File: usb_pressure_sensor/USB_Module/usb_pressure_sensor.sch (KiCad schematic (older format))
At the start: 8 parts, among them IC1 STM32F042F6P6, J1 SCREW_TERM, J2 MODULE_BRIDGE, P1 SWD_TC, U1 MICRO_USB

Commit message: Started update to different pressure sensor module
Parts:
- removed J1: SCREW_TERM, symbol CONN_01x02
- added C2: 1u, Capacitors_SMD:C_0603, symbol C
- added IC2: MCP1700, agg:SOT-23, symbol MCP1700
- added R3: 10k, Resistors_THT:R_Axial_DIN0207_L6.3mm_D2.5mm_P7.62mm_Horizontal, symbol R
- added SW1: SWITCH_SPST, symbol SWITCH_SPST
- C1: value 22u -> 1u; footprint (none) -> Capacitors_SMD:C_0603
- J2: footprint (none) -> Socket_Strips:Socket_Strip_Straight_2x03_Pitch2.54mm
- P1: footprint agg:TC2030-NL -> footprints:SWD_CONN
- R1, R2: footprint (none) -> Resistors_THT:R_Axial_DIN0207_L6.3mm_D2.5mm_P7.62mm_Horizontal
- U1: footprint (none) -> agg:MICROUSB_MOLEX_47589-0001
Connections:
- net labels added: 3v3, 5v
- net labels removed: VDD, VSS
- wire segments 25 -> 32
- no-connect marks 13 -> 11
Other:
- note added: "Capacitor should be as \nclose as possible to VOUT pin\n"
- note removed: "Need a value small enough so we \ncan have surface mount but large \nenough to be useful as a bypass\ncapacitor"
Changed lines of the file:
@@
 $EndComp
 Text Label 6150 1300 0    60   ~ 0
-VDD
+3v3
 Text Label 6150 1400 0    60   ~ 0
-VDD
+3v3
 Text Label 6150 1500 0    60   ~ 0
 GND
@@
 NoConn ~ 6400 2200
 NoConn ~ 6400 2300
-NoConn ~ 6400 2000
 NoConn ~ 6400 1900
 $Comp
@@
 F 0 "P1" H 6700 3450 50  0000 L CNN
 F 1 "SWD_TC" H 6700 3050 50  0000 L CNN
-F 2 "agg:TC2030-NL" H 6700 2950 50  0001 L CNN
+F 2 "footprints:SWD_CONN" H 6700 2950 50  0001 L CNN
 F 3 "" H 6600 3350 50  0001 C CNN
 	1    7000 3250
@@
 $EndComp
 Text Label 6600 3150 2    60   ~ 0
-VDD
+3v3
 Text Label 6600 3250 2    60   ~ 0
 NRST
@@
 NoConn ~ 7400 3350
 $Comp
-L CONN_01x02 J1
-U 1 1 59921283
-P 3400 2050
-F 0 "J1" H 3350 2150 50  0000 L CNN
-F 1 "SCREW_TERM" H 3350 1850 50  0000 L CNN
-F 2 "" H 3400 2050 50  0001 C CNN
-F 3 "" H 3400 2050 50  0001 C CNN
-	1    3400 2050
-	1    0    0    -1
-$EndComp
-Text Label 3550 2050 0    60   ~ 0
-VDD
-Text Label 3550 2150 0    60   ~ 0
-VSS
-$Comp
-L C C1
-U 1 1 5992153B
-P 4000 2100
-F 0 "C1" H 4025 2200 50  0000 L CNN
-F 1 "22u" H 4025 2000 50  0000 L CNN
-F 2 "" H 4038 1950 50  0001 C CNN
-F 3 "" H 4000 2100 50  0001 C CNN
-	1    4000 2100
-	1    0    0    -1
-$EndComp
-Text Notes 4200 2300 0    60   ~ 0
-Need a value small enough so we \ncan have surface mount but large \nenough to be useful as a bypass\ncapacitor
-$Comp
 L MICRO_USB U1
 U 1 1 59922B96
@@
 F 0 "U1" H 3300 4000 60  0000 C CNN
 F 1 "MICRO_USB" H 3500 3400 60  0000 C CNN
-F 2 "" H 3350 3700 60  0001 C CNN
+F 2 "agg:MICROUSB_MOLEX_47589-0001" H 3350 3700 60  0001 C CNN
 F 3 "" H 3350 3700 60  0001 C CNN
 	1    3350 3700
 	1    0    0    -1
 $EndComp
-NoConn ~ 3650 3500
 NoConn ~ 3650 3800
 Text Label 3700 3900 0    60   ~ 0
@@
 F 0 "R1" V 3880 3600 50  0000 C CNN
 F 1 "22" V 3800 3600 50  0000 C CNN
-F 2 "" V 3730 3600 50  0001 C CNN
+F 2 "Resistors_THT:R_Axial_DIN0207_L6.3mm_D2.5mm_P7.62mm_Horizontal" V 3730 3600 50  0001 C CNN
 F 3 "" H 3800 3600 50  0001 C CNN
 	1    3800 3600
@@
 F 0 "R2" V 3880 3700 50  0000 C CNN
 F 1 "22" V 3800 3700 50  0000 C CNN
-F 2 "" V 3730 3700 50  0001 C CNN
+F 2 "Resistors_THT:R_Axial_DIN0207_L6.3mm_D2.5mm_P7.62mm_Horizontal" V 3730 3700 50  0001 C CNN
 F 3 "" H 3800 3700 50  0001 C CNN
 	1    3800 3700
@@
 F 0 "J2" H 9100 2150 50  0000 L CNN
 F 1 "MODULE_BRIDGE" H 9100 1750 50  0000 L CNN
-F 2 "" H 9200 2050 50  0001 C CNN
+F 2 "Socket_Strips:Socket_Strip_Straight_2x03_Pitch2.54mm" H 9200 2050 50  0001 C CNN
 F 3 "" H 9200 2050 50  0001 C CNN
 	1    9200 2050
 	1    0    0    -1
 $EndComp
-Wire Wire Line
-	6150 1500 6400 1500
-Wire Wire Line
-	6400 1300 6150 1300
-Wire Wire Line
-	6400 1400 6150 1400
-Wire Wire Line
-	6400 1700 6150 1700
-Wire Wire Line
-	7600 1800 8000 1800
-Wire Wire Line
-	7600 1900 8000 1900
-Wire Wire Line
-	7600 2000 8000 2000
-Wire Wire Line
-	7600 2400 8000 2400
-Wire Wire Line
-	7600 2500 8000 2500
-Wire Wire Line
-	7600 2200 8000 2200
-Wire Wire Line
-	7600 2300 8000 2300
-Wire Wire Line
-	3500 2050 3850 2050
-Wire Wire Line
-	3500 2150 3850 2150
-Wire Wire Line
-	3850 2050 3850 1950
-Wire Wire Line
-	3850 1950 4000 1950
-Wire Wire Line
-	3850 2150 3850 2250
-Wire Wire Line
-	3850 2250 4000 2250
-Wire Wire Line
-	3650 3900 3900 3900
-Wire Wire Line
-	3950 3600 4100 3600
-Wire Wire Line
-	3950 3700 4100 3700
 Text Label 8800 2050 0    60   ~ 0
-VDD
+3v3
 Text Label 8550 2150 0    60   ~ 0
 SPI_SCLK
@@
 Text Label 9350 2150 0    60   ~ 0
 SPI_MISO
+NoConn ~ 9300 2250
+$Comp
+L SWITCH_SPST SW1
+U 1 1 599811CC
+P 5750 2000
+F 0 "SW1" H 5750 2150 50  0000 C CNN
+F 1 "SWITCH_SPST" H 5750 1900 50  0000 C CNN
+F 2 "" H 5750 2000 50  0001 C CNN
+F 3 "" H 5750 2000 50  0001 C CNN
+	1    5750 2000
+	1    0    0    -1
+$EndComp
+$Comp
+L R R3
+U 1 1 59981239
+P 6100 2300
+F 0 "R3" V 6180 2300 50  0000 C CNN
+F 1 "10k" V 6100 2300 50  0000 C CNN
+F 2 "Resistors_THT:R_Axial_DIN0207_L6.3mm_D2.5mm_P7.62mm_Horizontal" V 6030 2300 50  0001 C CNN
+F 3 "" H 6100 2300 50  0001 C CNN
+	1    6100 2300
+	1    0    0    -1
+$EndComp
+Text Label 6100 2600 0    60   ~ 0
+GND
+Text Label 5400 2000 0    60   ~ 0
+3v3
+$Comp
+L MCP1700 IC2
+U 1 1 59982B20
+P 3550 2400
+F 0 "IC2" H 3350 2500 50  0000 L CNN
+F 1 "MCP1700" H 3350 2200 50  0000 L CNN
+F 2 "agg:SOT-23" H 3350 2100 50  0001 L CNN
+F 3 "http://www.farnell.com/datasheets/1784514.pdf" H 3350 2000 50  0001 L CNN
+F 4 "1296592" H 3350 1900 50  0001 L CNN "Farnell"
+	1    3550 2400
+	1    0    0    -1
+$EndComp
+$Comp
+L C C2
+U 1 1 59982B76
+P 4050 2600
+F 0 "C2" H 4075 2700 50  0000 L CNN
+F 1 "1u" H 4075 2500 50  0000 L CNN
+F 2 "Capacitors_SMD:C_0603" H 4088 2450 50  0001 C CNN
+F 3 "" H 4050 2600 50  0001 C CNN
+	1    4050 2600
+	1    0    0    -1
+$EndComp
+Text Label 4050 2900 0    60   ~ 0
+GND
+Text Notes 4250 2700 0    60   ~ 0
+Capacitor should be as \nclose as possible to VOUT pin\n
+Text Label 3250 2750 0    60   ~ 0
+GND
+$Comp
+L C C1
+U 1 1 5998353C
+P 3000 2550
+F 0 "C1" H 3025 2650 50  0000 L CNN
+F 1 "1u" H 3025 2450 50  0000 L CNN
+F 2 "Capacitors_SMD:C_0603" H 3038 2400 50  0001 C CNN
+F 3 "" H 3000 2550 50  0001 C CNN
+	1    3000 2550
+	1    0    0    -1
+$EndComp
+Text Label 2600 2400 0    60   ~ 0
+5v
+Text Label 4250 2400 0    60   ~ 0
+3v3
+Wire Wire Line
+	6150 1500 6400 1500
+Wire Wire Line
+	6400 1300 6150 1300
+Wire Wire Line
+	6400 1400 6150 1400
+Wire Wire Line
+	6400 1700 6150 1700
+Wire Wire Line
+	7600 1800 8000 1800
+Wire Wire Line
+	7600 1900 8000 1900
+Wire Wire Line
+	7600 2000 8000 2000
+Wire Wire Line
+	7600 2400 8000 2400
+Wire Wire Line
+	7600 2500 8000 2500
+Wire Wire Line
+	7600 2200 8000 2200
+Wire Wire Line
+	7600 2300 8000 2300
+Wire Wire Line
+	3650 3900 3900 3900
+Wire Wire Line
+	3950 3600 4100 3600
+Wire Wire Line
+	3950 3700 4100 3700
 Wire Wire Line
 	9300 2150 9750 2150
@@
 Wire Wire Line
 	9000 2250 8550 2250
-NoConn ~ 9300 2250
+Wire Wire Line
+	5850 2000 6400 2000
+Wire Wire Line
+	6100 2000 6100 2150
+Connection ~ 6100 2000
+Wire Wire Line
+	6100 2450 6100 2600
+Wire Wire Line
+	5650 2000 5400 2000
+Wire Wire Line
+	3950 2400 4250 2400
+Wire Wire Line
+	4050 2400 4050 2450
+Wire Wire Line
+	4050 2750 4050 2900
+Wire Wire Line
+	3250 2500 3250 2750
+Wire Wire Line
+	2600 2400 3250 2400
+Wire Wire Line
+	3000 2700 3000 2750
+Wire Wire Line
+	3000 2750 3250 2750
+Connection ~ 3000 2400
+Connection ~ 4050 2400
+Wire Wire Line
+	3650 3500 3650 3450
+Wire Wire Line
+	3650 3450 4000 3450
+Text Label 4000 3450 0    60   ~ 0
+5v
 $EndSCHEMATC

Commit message: First iteration with new pressure sensor
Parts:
- added C3, C4: 24p, symbol C
- added R4: 2.2M, symbol R
- added R5: 180k, symbol R
- added U2: SN74LVC1GX04, symbol SN74LVC1GX04
- added Y1: Crystal 32.768kHz, symbol Crystal
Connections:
- net labels added: DIN, DOUT, MCLK, SCLK
- net labels removed: SPI_MISO, SPI_MOSI, SPI_SCLK
- wire segments 32 -> 46
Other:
- note added: "Chose 22ohm because:\nhttp://www.eevblog.com/forum/projects/why-usb-data-series-resistors/"
- note added: "Crystal Oscillator"
- note added: "Crystal Oscillator design process:\n\nFor the values used http://www.ti.com/lit/an/szza043/szza043.pdf page 13\n180k should be approx equal to capacitave reactance of one of the capacitors\n connected to gound. Used 1/j*2pi*f*C where f is the resonant freq of the \ncrystal.\n2.2M should be between 1M and 10M so I just used the one they used in the\nexample.\nThe two caps going to ground should be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"
- note added: "I'm using the SPI pins even though the pressure sesnsor doesn't say it uses SPI\nbut it should be the same concepts right?\nEven if we can't hack SPI into working these pins are still general purpose IO so\ni think it's ok?"
- note added: "MCU"
- note added: "Module Bridge"
- note added: "Power Supply"
- note added: "Serial Wire Debugging"
- note added: "USB Interface"
- moved on the sheet: C1, C2, IC1, IC2, J2, P1, R1, R2, R3, SW1, U1

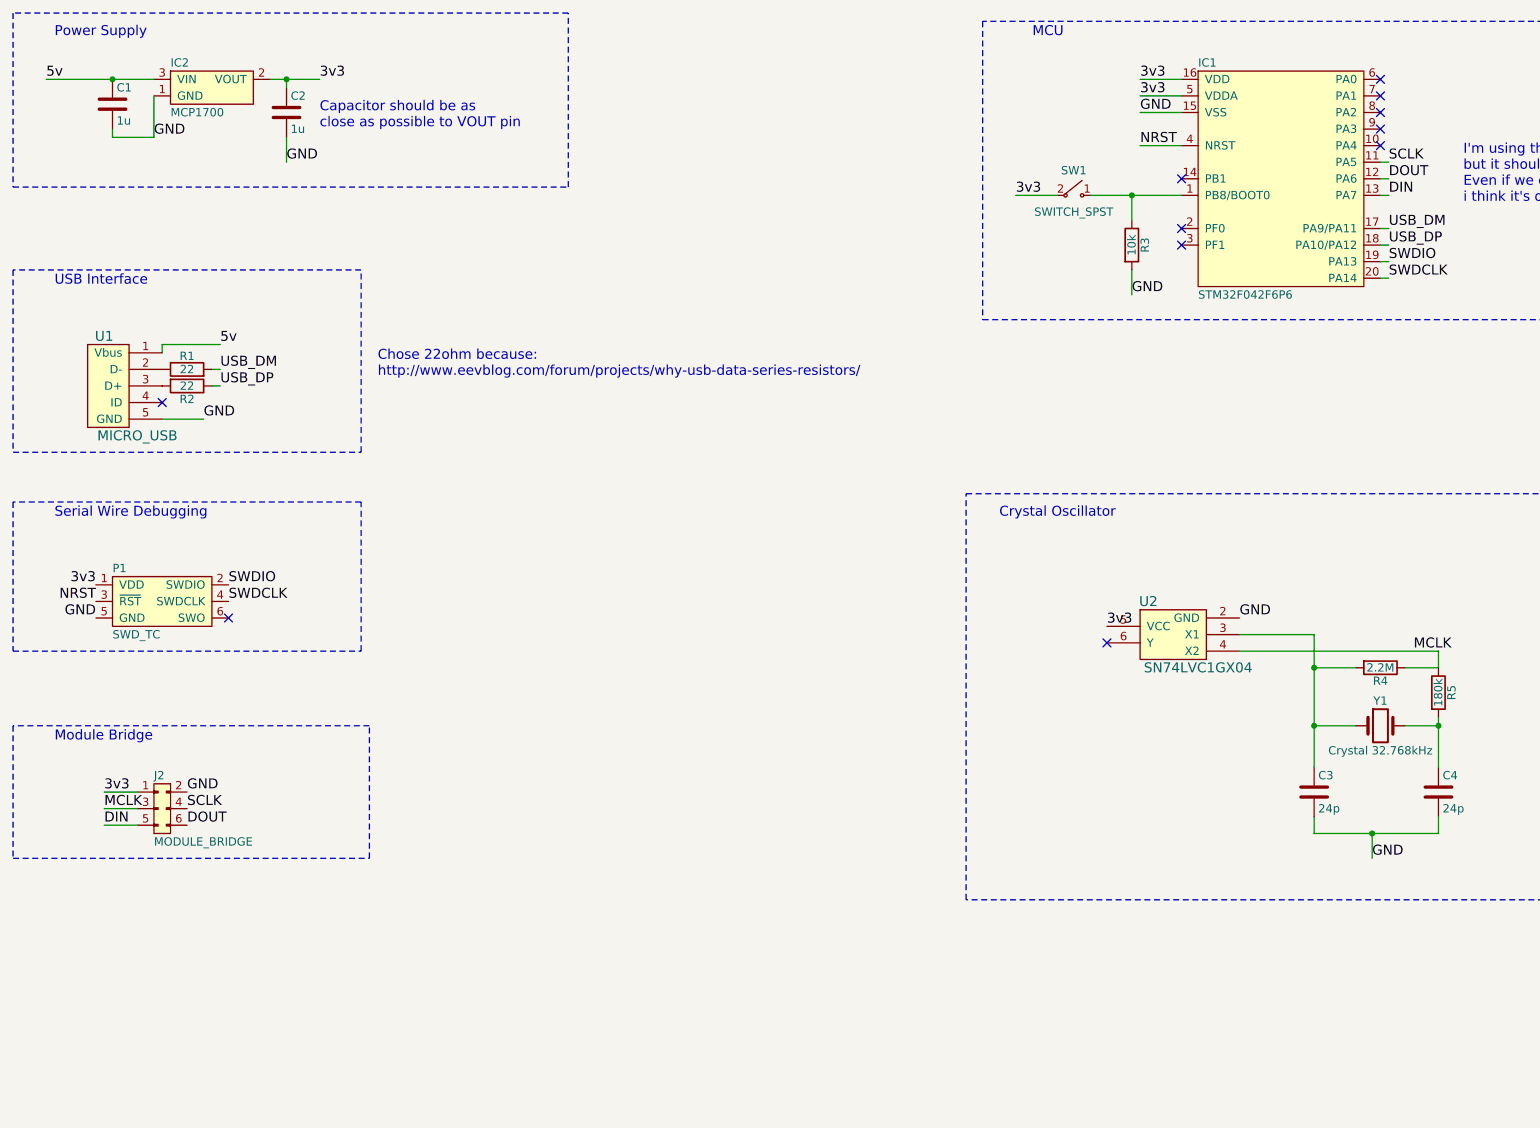
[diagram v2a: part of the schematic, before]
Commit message: added pin header to all pins on the MCU
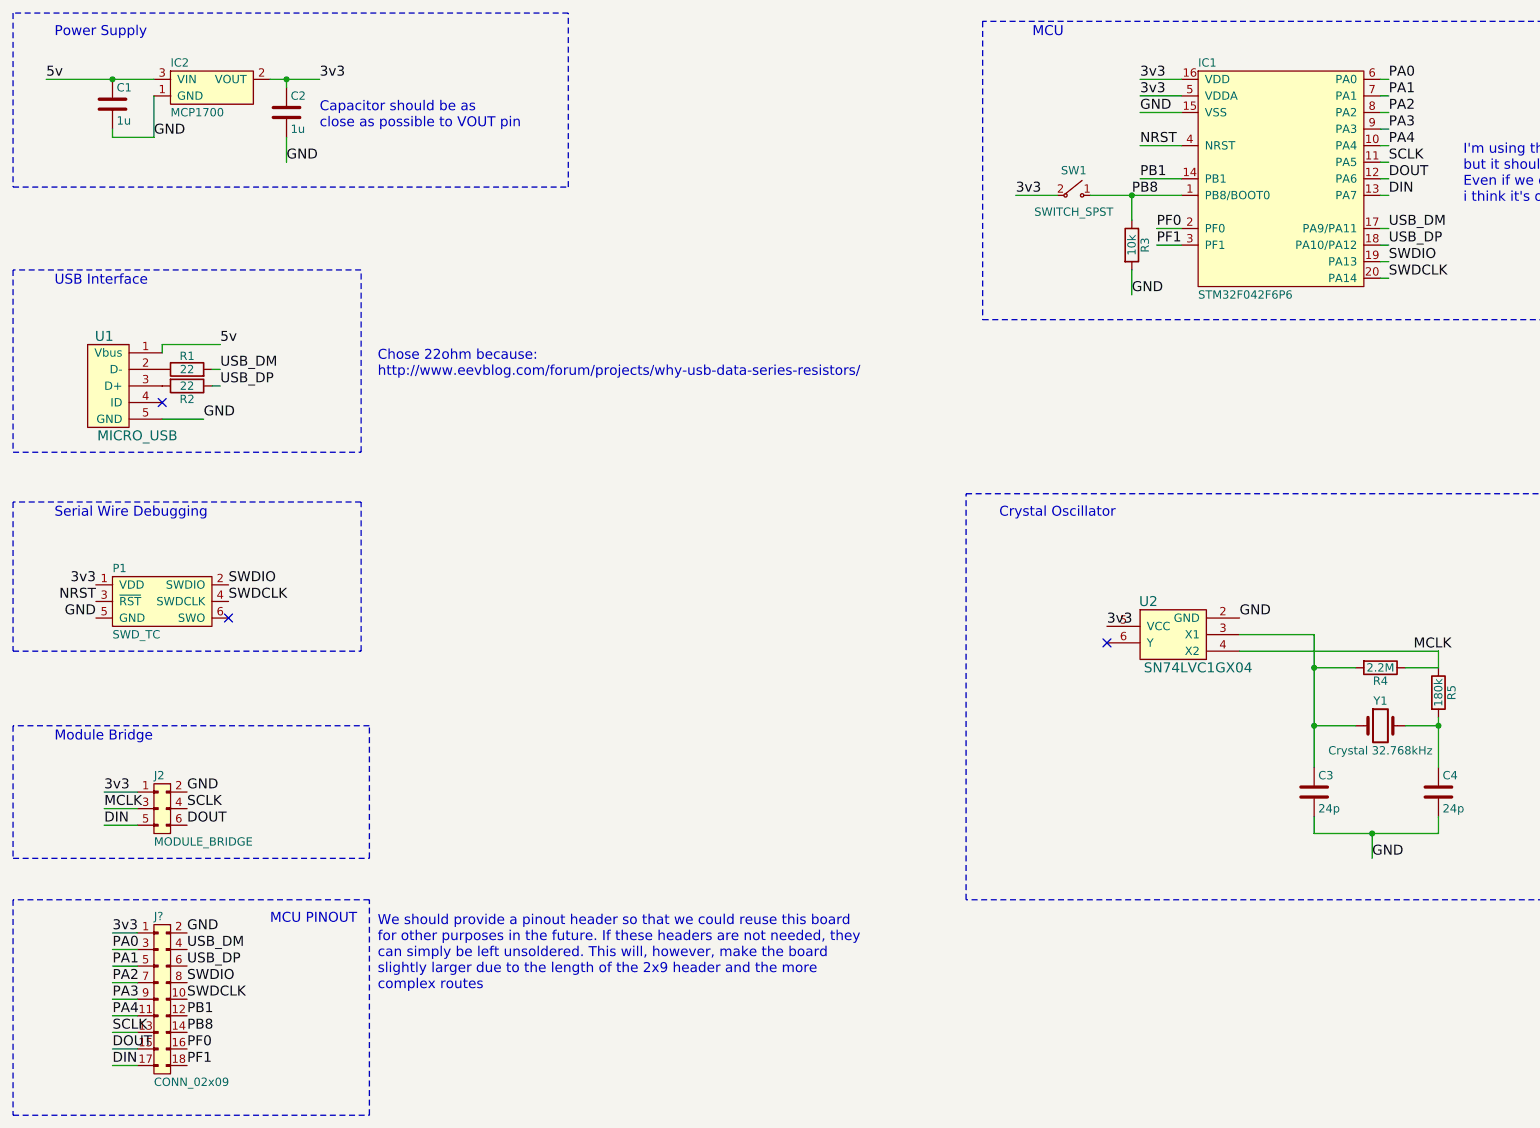
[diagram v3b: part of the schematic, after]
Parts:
- added J?: CONN_02x09, symbol CONN_02x09
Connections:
- net 3v3: now also J?.1
- net DIN: now also J?.17
- net DOUT: now also J?.15
- net GND: now also J?.2
- net SCLK: now also J?.13
- net SWDCLK: now also J?.10
- net SWDIO: now also J?.8
- net USB_DM: now also J?.4
- net USB_DP: now also J?.6
- net PB8: now reaches IC1.1 (PB8/BOOT0), R3.1, SW1.1 ("~")
- net PB8: now also J?.14
- net PA4: now reaches IC1.10 (PA4)
- net PA4: now also J?.11
- net PB1: now reaches IC1.14 (PB1)
- net PB1: now also J?.12
- net PF0: now reaches IC1.2 (PF0)
- net PF0: now also J?.16
- net PF1: now reaches IC1.3 (PF1)
- net PF1: now also J?.18
- net PA0: now reaches IC1.6 (PA0)
- net PA0: now also J?.3
- net PA1: now reaches IC1.7 (PA1)
- net PA1: now also J?.5
- net PA2: now reaches IC1.8 (PA2)
- net PA2: now also J?.7
- net PA3: now reaches IC1.9 (PA3)
- net PA3: now also J?.9
- no-connect marks 11 -> 3
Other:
- note added: "MCU PINOUT"
- note added: "We should provide a pinout header so that we could reuse this board \nfor other purposes in the future. If these headers are not needed, they\ncan simply be left unsoldered. This will, however, make the board \nslightly larger due to the length of the 2x9 header and the more \ncomplex routes\n"
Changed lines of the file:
@@
 Comment4 ""
 $EndDescr
-$Comp
-L STM32F0xxFxPx IC1
-U 1 1 5990B64E
-P 9150 1850
-F 0 "IC1" H 8650 2550 50  0000 L CNN
-F 1 "STM32F042F6P6" H 8650 1150 50  0000 L CNN
-F 2 "agg:TSSOP-20" H 8650 1050 50  0001 L CNN
-F 3 "http://www.st.com/st-web-ui/static/active/en/resource/technical/document/datasheet/DM00105814.pdf" H 8650 950 50  0001 L CNN
-F 4 "2469549" H 8650 850 50  0001 L CNN "Farnell"
-	1    9150 1850
-	1    0    0    -1
-$EndComp
 Text Label 8300 1250 0    60   ~ 0
 3v3
@@
 Text Label 8300 1650 0    60   ~ 0
 NRST
-NoConn ~ 9750 1250
-NoConn ~ 9750 1350
-NoConn ~ 9750 1450
-NoConn ~ 9750 1550
-NoConn ~ 9750 1650
 Text Label 9800 2350 0    60   ~ 0
 SWDIO
@@
 Text Label 9800 1950 0    60   ~ 0
 DIN
-NoConn ~ 8550 2150
-NoConn ~ 8550 2250
-NoConn ~ 8550 1850
 $Comp
 L SWD_TC P1
@@
 Text Notes 10250 2000 0    60   ~ 0
 I'm using the SPI pins even though the pressure sesnsor doesn't say it uses SPI\nbut it should be the same concepts right?\nEven if we can't hack SPI into working these pins are still general purpose IO so\ni think it's ok?
+$Comp
+L STM32F0xxFxPx IC1
+U 1 1 5990B64E
+P 9150 1850
+F 0 "IC1" H 8650 2550 50  0000 L CNN
+F 1 "STM32F042F6P6" H 8650 1150 50  0000 L CNN
+F 2 "agg:TSSOP-20" H 8650 1050 50  0001 L CNN
+F 3 "http://www.st.com/st-web-ui/static/active/en/resource/technical/document/datasheet/DM00105814.pdf" H 8650 950 50  0001 L CNN
+F 4 "2469549" H 8650 850 50  0001 L CNN "Farnell"
+	1    9150 1850
+	1    0    0    -1
+$EndComp
+Wire Wire Line
+	8300 1850 8550 1850
+Wire Wire Line
+	8550 2150 8400 2150
+Wire Wire Line
+	8550 2250 8400 2250
+Wire Wire Line
+	9750 1250 9800 1250
+Wire Wire Line
+	9750 1350 9800 1350
+Wire Wire Line
+	9750 1450 9800 1450
+Wire Wire Line
+	9750 1550 9800 1550
+Wire Wire Line
+	9750 1650 9800 1650
+Text Label 8300 1850 0    60   ~ 0
+PB1
+Text Label 8400 2150 0    60   ~ 0
+PF0
+Text Label 8400 2250 0    60   ~ 0
+PF1
+Text Label 9800 1250 0    60   ~ 0
+PA0
+Text Label 9800 1350 0    60   ~ 0
+PA1
+Text Label 9800 1450 0    60   ~ 0
+PA2
+Text Label 9800 1550 0    60   ~ 0
+PA3
+Text Label 9800 1650 0    60   ~ 0
+PA4
+Wire Notes Line
+	1500 6200 1500 7500
+Wire Notes Line
+	1500 7500 3650 7500
+Wire Notes Line
+	3650 7500 3650 6200
+Wire Notes Line
+	3650 6200 1500 6200
+$Comp
+L CONN_02x09 J?
+U 1 1 599B5AC0
+P 2450 6400
+F 0 "J?" H 2350 6500 50  0000 L CNN
+F 1 "CONN_02x09" H 2350 5500 50  0000 L CNN
+F 2 "" H 2450 6400 50  0001 C CNN
+F 3 "" H 2450 6400 50  0001 C CNN
+	1    2450 6400
+	1    0    0    -1
+$EndComp
+Text Notes 3050 6350 0    60   ~ 0
+MCU PINOUT
+Wire Wire Line
+	2100 6400 2250 6400
+Wire Wire Line
+	2100 6500 2250 6500
+Wire Wire Line
+	2250 6600 2100 6600
+Wire Wire Line
+	2100 6700 2250 6700
+Wire Wire Line
+	2250 6800 2100 6800
+Wire Wire Line
+	2100 6900 2250 6900
+Wire Wire Line
+	2250 7000 2100 7000
+Wire Wire Line
+	2100 7100 2250 7100
+Wire Wire Line
+	2250 7200 2100 7200
+Text Label 2100 6400 0    60   ~ 0
+3v3
+Text Label 2550 6400 0    60   ~ 0
+GND
+Text Label 2100 6500 0    60   ~ 0
+PA0
+Text Label 2100 6600 0    60   ~ 0
+PA1
+Text Label 2100 6700 0    60   ~ 0
+PA2
+Text Label 2100 6800 0    60   ~ 0
+PA3
+Text Label 2100 6900 0    60   ~ 0
+PA4
+Text Label 2100 7000 0    60   ~ 0
+SCLK
+Text Label 2100 7100 0    60   ~ 0
+DOUT
+Text Label 2100 7200 0    60   ~ 0
+DIN
+Text Label 2550 6500 0    60   ~ 0
+USB_DM
+Text Label 2550 6600 0    60   ~ 0
+USB_DP
+Text Label 2550 6700 0    60   ~ 0
+SWDIO
+Text Label 2550 6800 0    60   ~ 0
+SWDCLK
+Text Label 2550 6900 0    60   ~ 0
+PB1
+Text Label 8250 1950 0    60   ~ 0
+PB8
+Text Label 2550 7000 0    60   ~ 0
+PB8
+Text Label 2550 7100 0    60   ~ 0
+PF0
+Text Label 2550 7200 0    60   ~ 0
+PF1
+Text Notes 3700 6750 0    60   ~ 0
+We should provide a pinout header so that we could reuse this board \nfor other purposes in the future. If these headers are not needed, they\ncan simply be left unsoldered. This will, however, make the board \nslightly larger due to the length of the 2x9 header and the more \ncomplex routes\n
 $EndSCHEMATC
